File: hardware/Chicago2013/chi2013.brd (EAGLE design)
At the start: 35.6 x 31.8 mm, 9 parts, among them IC1 TINY24/44/84-SSU, J1 AVR_SPI_PRG_6NS

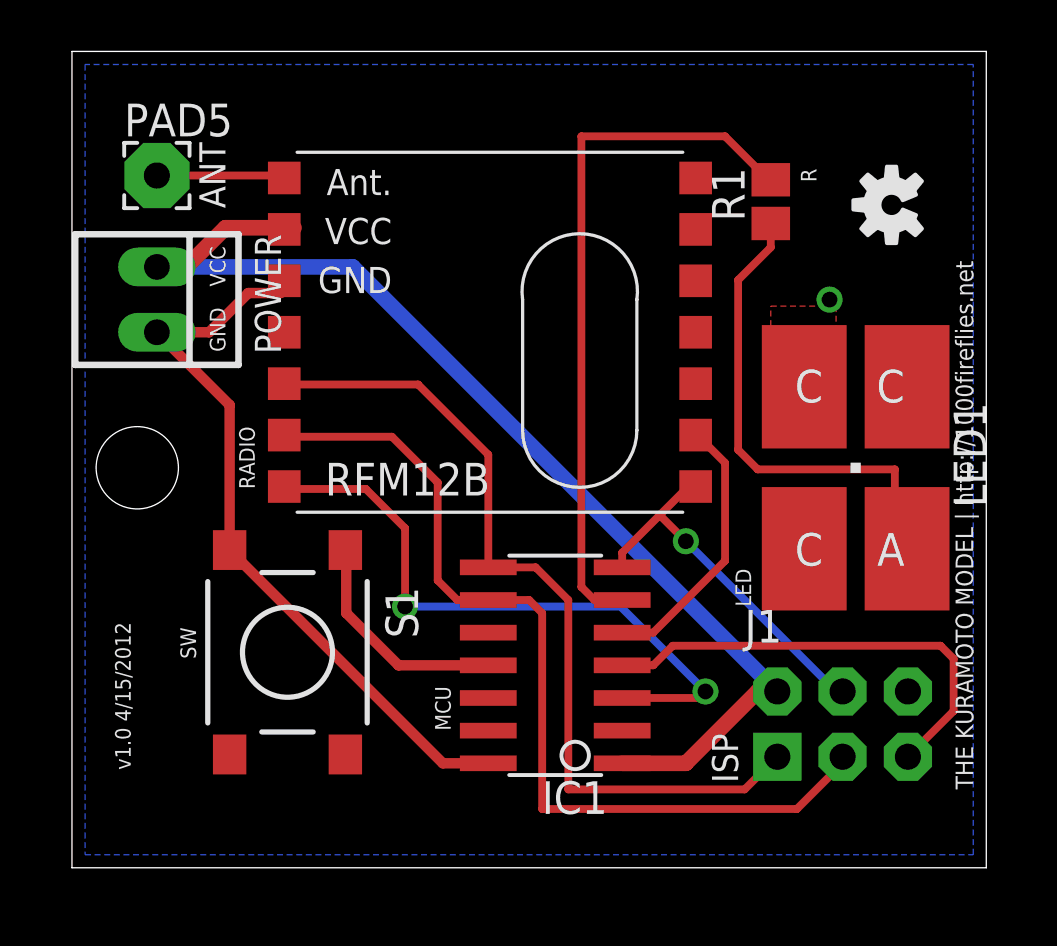
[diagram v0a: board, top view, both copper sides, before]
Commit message: Removed old revisions and added two new ones. General repo cleanup.
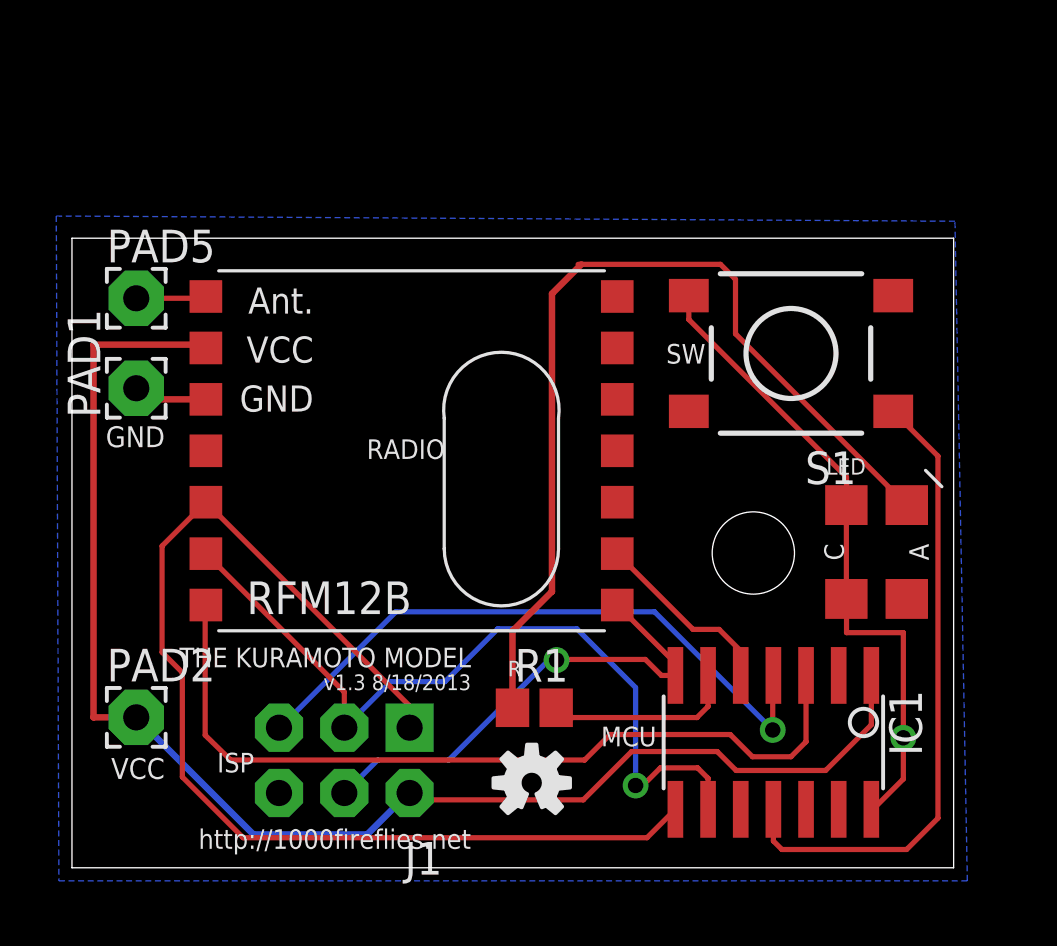
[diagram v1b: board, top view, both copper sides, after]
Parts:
- removed LED1: CLM4B-RKW-CWaXbAA3, led:P-LCC-4
- removed POWER: 22-23-2021, con-molex:22-23-2021
- added PAD1: GND, wirepad:2,15/1,0
- added PAD2: VCC, wirepad:2,15/1,0
- added U$3: Avago 630-ALMD-EG3D-VX002, ALMD-XX3D:ALMD-**3D
- IC1: value TINY24/44/84-SSU -> Atmel ATtiny84a-SSU
- PAD5: device wirepad:2,54/1,0 -> wirepad:2,15/1,0
- R1: value 18 ohm -> 30 ohm
- RFM12B: value RFM12BN -> HopeRF RFM12B-433S1
- S1: value DTSM-6 -> Mountain Switch 101-0364-EV
- moved U$1 26.5 mm to (17.9, 3.30), turned to 0 degrees
- moved S1 22.8 mm to (28.0, 20.0), turned to 180 degrees
- moved R1 21.7 mm to (18.0, 6.22), turned to 0 degrees
- moved J1 19.4 mm to (10.6, 4.18), turned to 180 degrees
- moved IC1 9.00 mm to (27.3, 4.88), turned to 180 degrees
- moved RFM12B 5.53 mm to (13.2, 16.2)
- moved PAD5 4.84 mm to (2.50, 22.1)
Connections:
- net GND: now also PAD1.1, S1.4, U$3.C1, U$3.C2; no longer LED1.C@4, POWER.2, S1.3
- net N$1: now also U$3.A1; no longer LED1.A
- net VCC: now also PAD2.1; no longer POWER.1
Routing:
- net N$6: track 27.4 -> 7.40 mm
- net N$1: track 19.1 -> 36.3 mm
- net N$10: track 8.83 -> 24.8 mm
- net N$3: track 33.1 -> 44.4 mm
- net VCC: track 45.0 -> 55.6 mm
- net N$5: track 24.8 -> 32.4 mm, vias 2 -> 0
- net N$14: track 18.0 -> 25.1 mm, vias 0 -> 1
- net N$4: track 14.4 -> 19.0 mm
- net N$2: track 35.4 -> 31.3 mm, vias 0 -> 1
- net N$7: track 10.5 -> 7.32 mm
- net N$8: track 4.99 -> 2.74 mm
- net GND: track 29.8 -> 28.4 mm
- removed copper zone on layer 1, net GND
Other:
- board size 35.6 x 31.8 mm -> 34.3 x 24.5 mm
- board text added: "THE KURAMOTO MODEL"
- board text added: "http://1000fireflies.net"
- board text added: "v1.3 8/18/2013"
- board text removed: "ANT"
- board text removed: "THE KURAMOTO MODEL | http://1000fireflies.net"
- board text removed: "v1.0 4/15/2012"
